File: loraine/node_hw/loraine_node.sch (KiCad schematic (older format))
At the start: 39 parts, among them CON1 BARREL_JACK, IC1 ATTINY2313A-S, P1 MOLEX, P2 MOLEX, P3 SOLDER_PAD, P4 ICSP, P5 OUTPUTS, P6 BUS, Q1 FZT600, Q2 FZT600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

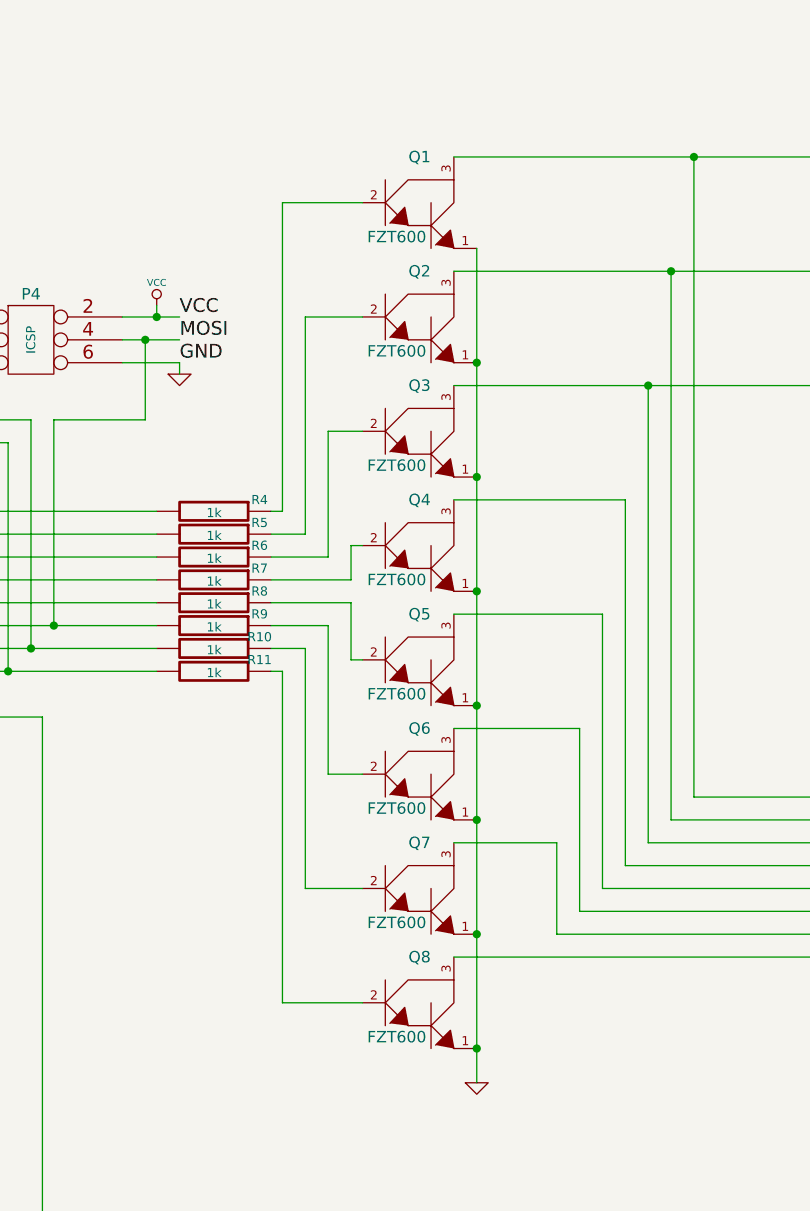
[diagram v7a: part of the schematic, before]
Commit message: Changed darlingtons to PTH part
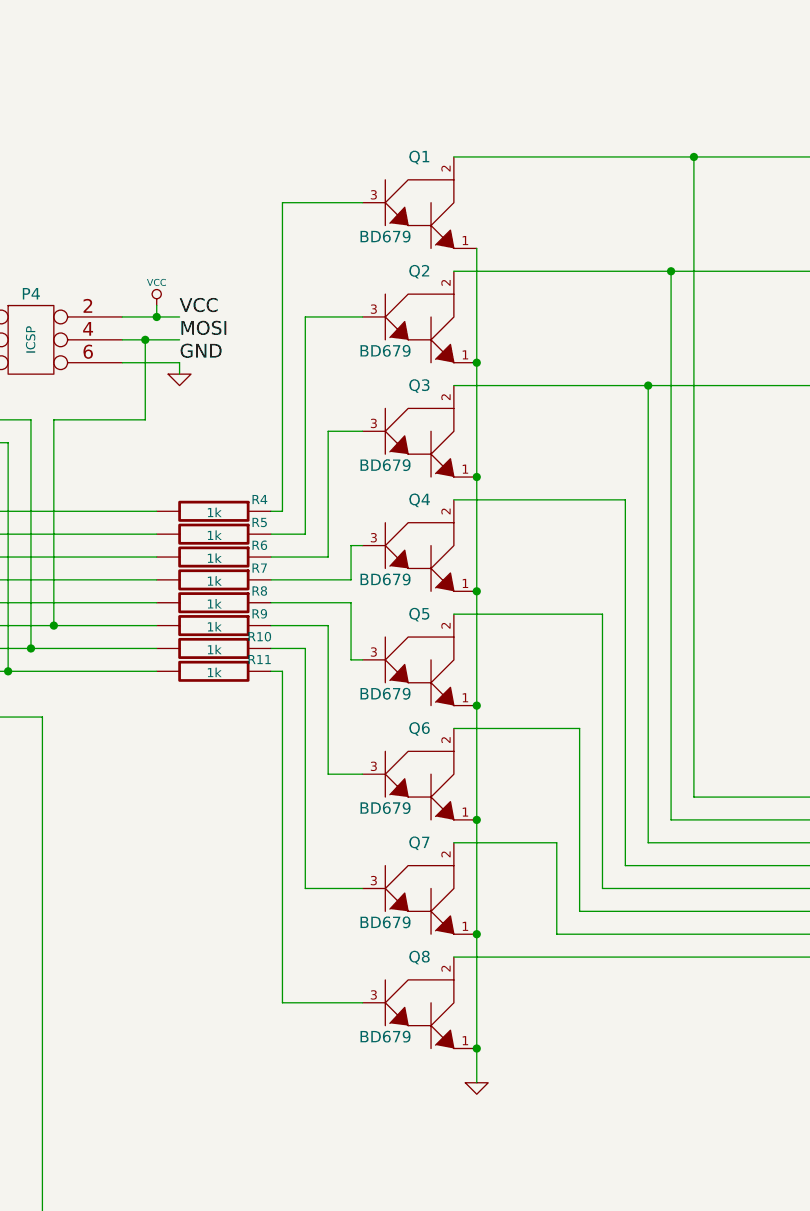
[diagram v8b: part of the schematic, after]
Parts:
- removed Q1, Q2, Q3, Q4, Q5, Q6, Q7, Q8: FZT600, symbol DARL_N
- added Q1, Q2, Q3, Q4, Q5, Q6, Q7, Q8: BD679, symbol BD679
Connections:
- net GND: now also Q1.1, Q2.1, Q3.1, Q4.1, Q5.1, Q6.1, Q7.1, Q8.1
- net at R4.1: now also Q1.3
- net at D1.2 (K), P5.1: now also Q1.2
- net at R5.1: now also Q2.3
- net at R6.1: now also Q3.3
- net at R7.1: now also Q4.3
- net at R8.1: now also Q5.3
- net at R9.1: now also Q6.3
- net at R10.1: now also Q7.3
- net at R11.1: now also Q8.3
- net at D2.2 (K), P5.3: now also Q2.2
- net at D3.2 (K), P5.5: now also Q3.2
- net at P5.7: now also Q4.2
- net at P5.9: now also Q5.2
- net at P5.11: now also Q6.2
- net at P5.13: now also Q7.2
- net at P5.15: now also Q8.2
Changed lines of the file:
@@
 LIBS:valves
 LIBS:sn65176bd
+LIBS:bd679
 LIBS:loraine_node-cache
 EELAYER 24 0
@@
 $EndComp
 $Comp
-L DARL_N Q1
-U 1 1 533876DD
-P 6750 2350
-F 0 "Q1" H 6750 2600 50  0000 C CNN
-F 1 "FZT600" H 6650 2250 50  0000 C CNN
-F 2 "" H 6750 2350 60  0000 C CNN
-F 3 "" H 6750 2350 60  0000 C CNN
-	1    6750 2350
-	1    0    0    -1
-$EndComp
-$Comp
 L R R4
 U 1 1 533877F8
@@
 Wire Wire Line
 	4800 4350 5600 4350
-$Comp
-L DARL_N Q2
-U 1 1 533882AD
-P 6750 2850
-F 0 "Q2" H 6750 3100 50  0000 C CNN
-F 1 "FZT600" H 6650 2750 50  0000 C CNN
-F 2 "" H 6750 2850 60  0000 C CNN
-F 3 "" H 6750 2850 60  0000 C CNN
-	1    6750 2850
-	1    0    0    -1
-$EndComp
-$Comp
-L DARL_N Q3
-U 1 1 533882C1
-P 6750 3350
-F 0 "Q3" H 6750 3600 50  0000 C CNN
-F 1 "FZT600" H 6650 3250 50  0000 C CNN
-F 2 "" H 6750 3350 60  0000 C CNN
-F 3 "" H 6750 3350 60  0000 C CNN
-	1    6750 3350
-	1    0    0    -1
-$EndComp
-$Comp
-L DARL_N Q4
-U 1 1 533882D5
-P 6750 3850
-F 0 "Q4" H 6750 4100 50  0000 C CNN
-F 1 "FZT600" H 6650 3750 50  0000 C CNN
-F 2 "" H 6750 3850 60  0000 C CNN
-F 3 "" H 6750 3850 60  0000 C CNN
-	1    6750 3850
-	1    0    0    -1
-$EndComp
 Wire Wire Line
 	6100 3650 6150 3650
@@
 	6150 3650 6150 2300
 Wire Wire Line
-	6150 2300 6500 2300
-Wire Wire Line
 	6100 3750 6250 3750
 Wire Wire Line
@@
 Wire Wire Line
 	6450 3800 6500 3800
-$Comp
-L DARL_N Q5
-U 1 1 53388410
-P 6750 4350
-F 0 "Q5" H 6750 4600 50  0000 C CNN
-F 1 "FZT600" H 6650 4250 50  0000 C CNN
-F 2 "" H 6750 4350 60  0000 C CNN
-F 3 "" H 6750 4350 60  0000 C CNN
-	1    6750 4350
-	1    0    0    -1
-$EndComp
-$Comp
-L DARL_N Q6
-U 1 1 53388424
-P 6750 4850
-F 0 "Q6" H 6750 5100 50  0000 C CNN
-F 1 "FZT600" H 6650 4750 50  0000 C CNN
-F 2 "" H 6750 4850 60  0000 C CNN
-F 3 "" H 6750 4850 60  0000 C CNN
-	1    6750 4850
-	1    0    0    -1
-$EndComp
-$Comp
-L DARL_N Q7
-U 1 1 53388438
-P 6750 5350
-F 0 "Q7" H 6750 5600 50  0000 C CNN
-F 1 "FZT600" H 6650 5250 50  0000 C CNN
-F 2 "" H 6750 5350 60  0000 C CNN
-F 3 "" H 6750 5350 60  0000 C CNN
-	1    6750 5350
-	1    0    0    -1
-$EndComp
-$Comp
-L DARL_N Q8
-U 1 1 5338844C
-P 6750 5850
-F 0 "Q8" H 6750 6100 50  0000 C CNN
-F 1 "FZT600" H 6650 5750 50  0000 C CNN
-F 2 "" H 6750 5850 60  0000 C CNN
-F 3 "" H 6750 5850 60  0000 C CNN
-	1    6750 5850
-	1    0    0    -1
-$EndComp
 Wire Wire Line
 	6100 4050 6450 4050
@@
 Wire Wire Line
 	6150 5800 6500 5800
-Wire Wire Line
-	7000 2500 7000 6150
 Connection ~ 7000 3000
 Connection ~ 7000 3500
@@
 	1    0    0    -1
 $EndComp
+$Comp
+L BD679 Q1
+U 1 1 5339A559
+P 6750 2350
+F 0 "Q1" H 6750 2600 50  0000 C CNN
+F 1 "BD679" H 6600 2250 50  0000 C CNN
+F 2 "" H 6750 2350 60  0000 C CNN
+F 3 "" H 6750 2350 60  0000 C CNN
+	1    6750 2350
+	1    0    0    -1
+$EndComp
+$Comp
+L BD679 Q2
+U 1 1 5339A577
+P 6750 2850
+F 0 "Q2" H 6750 3100 50  0000 C CNN
+F 1 "BD679" H 6600 2750 50  0000 C CNN
+F 2 "" H 6750 2850 60  0000 C CNN
+F 3 "" H 6750 2850 60  0000 C CNN
+	1    6750 2850
+	1    0    0    -1
+$EndComp
+$Comp
+L BD679 Q3
+U 1 1 5339A58B
+P 6750 3350
+F 0 "Q3" H 6750 3600 50  0000 C CNN
+F 1 "BD679" H 6600 3250 50  0000 C CNN
+F 2 "" H 6750 3350 60  0000 C CNN
+F 3 "" H 6750 3350 60  0000 C CNN
+	1    6750 3350
+	1    0    0    -1
+$EndComp
+$Comp
+L BD679 Q4
+U 1 1 5339A59F
+P 6750 3850
+F 0 "Q4" H 6750 4100 50  0000 C CNN
+F 1 "BD679" H 6600 3750 50  0000 C CNN
+F 2 "" H 6750 3850 60  0000 C CNN
+F 3 "" H 6750 3850 60  0000 C CNN
+	1    6750 3850
+	1    0    0    -1
+$EndComp
+$Comp
+L BD679 Q5
+U 1 1 5339A5B3
+P 6750 4350
+F 0 "Q5" H 6750 4600 50  0000 C CNN
+F 1 "BD679" H 6600 4250 50  0000 C CNN
+F 2 "" H 6750 4350 60  0000 C CNN
+F 3 "" H 6750 4350 60  0000 C CNN
+	1    6750 4350
+	1    0    0    -1
+$EndComp
+$Comp
+L BD679 Q6
+U 1 1 5339A5C7
+P 6750 4850
+F 0 "Q6" H 6750 5100 50  0000 C CNN
+F 1 "BD679" H 6600 4750 50  0000 C CNN
+F 2 "" H 6750 4850 60  0000 C CNN
+F 3 "" H 6750 4850 60  0000 C CNN
+	1    6750 4850
+	1    0    0    -1
+$EndComp
+$Comp
+L BD679 Q7
+U 1 1 5339A5DB
+P 6750 5350
+F 0 "Q7" H 6750 5600 50  0000 C CNN
+F 1 "BD679" H 6600 5250 50  0000 C CNN
+F 2 "" H 6750 5350 60  0000 C CNN
+F 3 "" H 6750 5350 60  0000 C CNN
+	1    6750 5350
+	1    0    0    -1
+$EndComp
+$Comp
+L BD679 Q8
+U 1 1 5339A5EF
+P 6750 5850
+F 0 "Q8" H 6750 6100 50  0000 C CNN
+F 1 "BD679" H 6600 5750 50  0000 C CNN
+F 2 "" H 6750 5850 60  0000 C CNN
+F 3 "" H 6750 5850 60  0000 C CNN
+	1    6750 5850
+	1    0    0    -1
+$EndComp
+Wire Wire Line
+	7000 2500 7000 6150
+Wire Wire Line
+	6150 2300 6500 2300
 $EndSCHEMATC
